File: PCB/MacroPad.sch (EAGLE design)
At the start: 42 parts, among them SW00 SWITCH-SMD-EVQP-P2602W, SW01 KEYSWITCH-PLAIN-MX-1U, SW02 KEYSWITCH-PLAIN-MX-1U, SW03 KEYSWITCH-PLAIN-MX-1U, SW04 KEYSWITCH-PLAIN-MX-1U, SW05 KEYSWITCH-PLAIN-MX-1U, SW06 KEYSWITCH-PLAIN-MX-1U, SW07 KEYSWITCH-PLAIN-MX-1U, SW08 KEYSWITCH-PLAIN-MX-1U, SW09 KEYSWITCH-PLAIN-MX-1U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

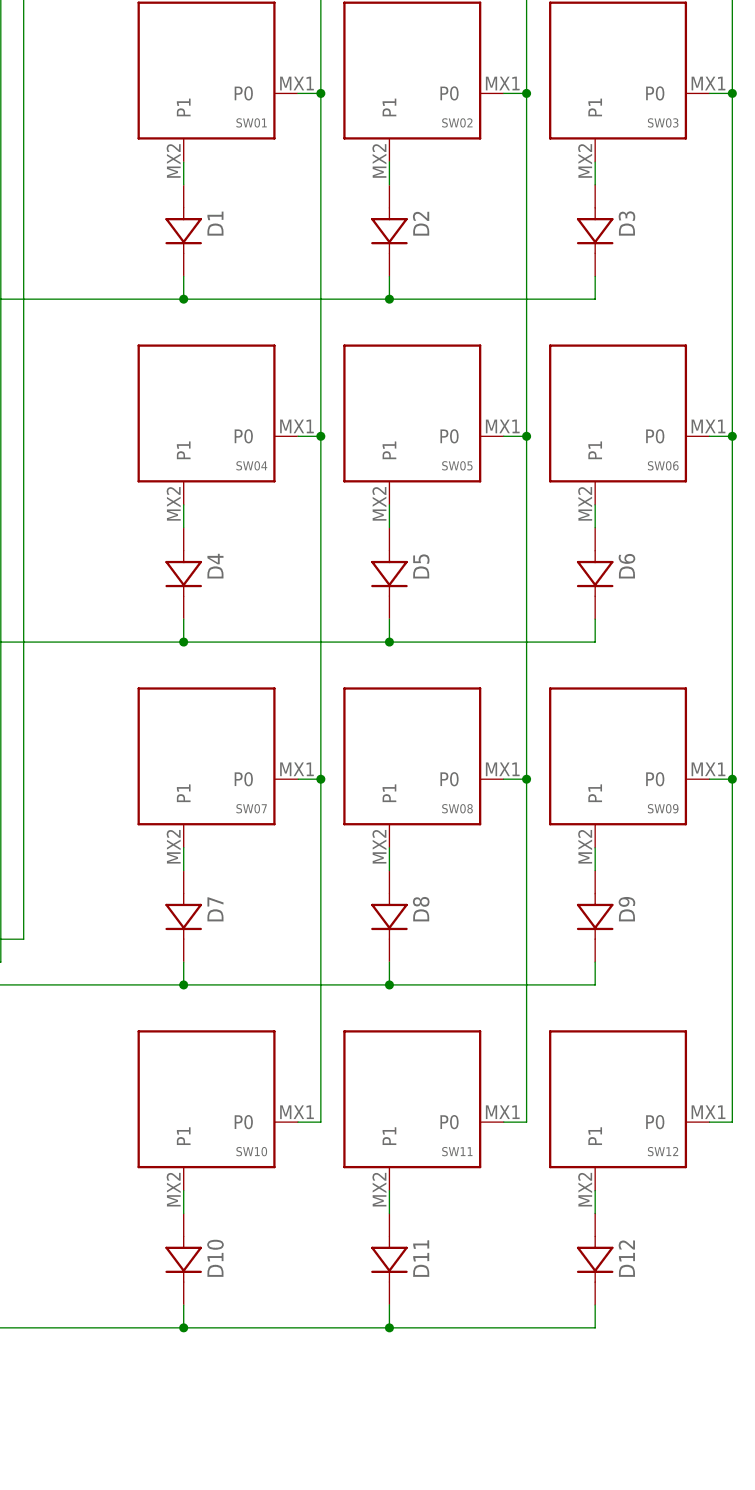
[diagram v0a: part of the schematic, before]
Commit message: Replace surface mount diodes with through hole
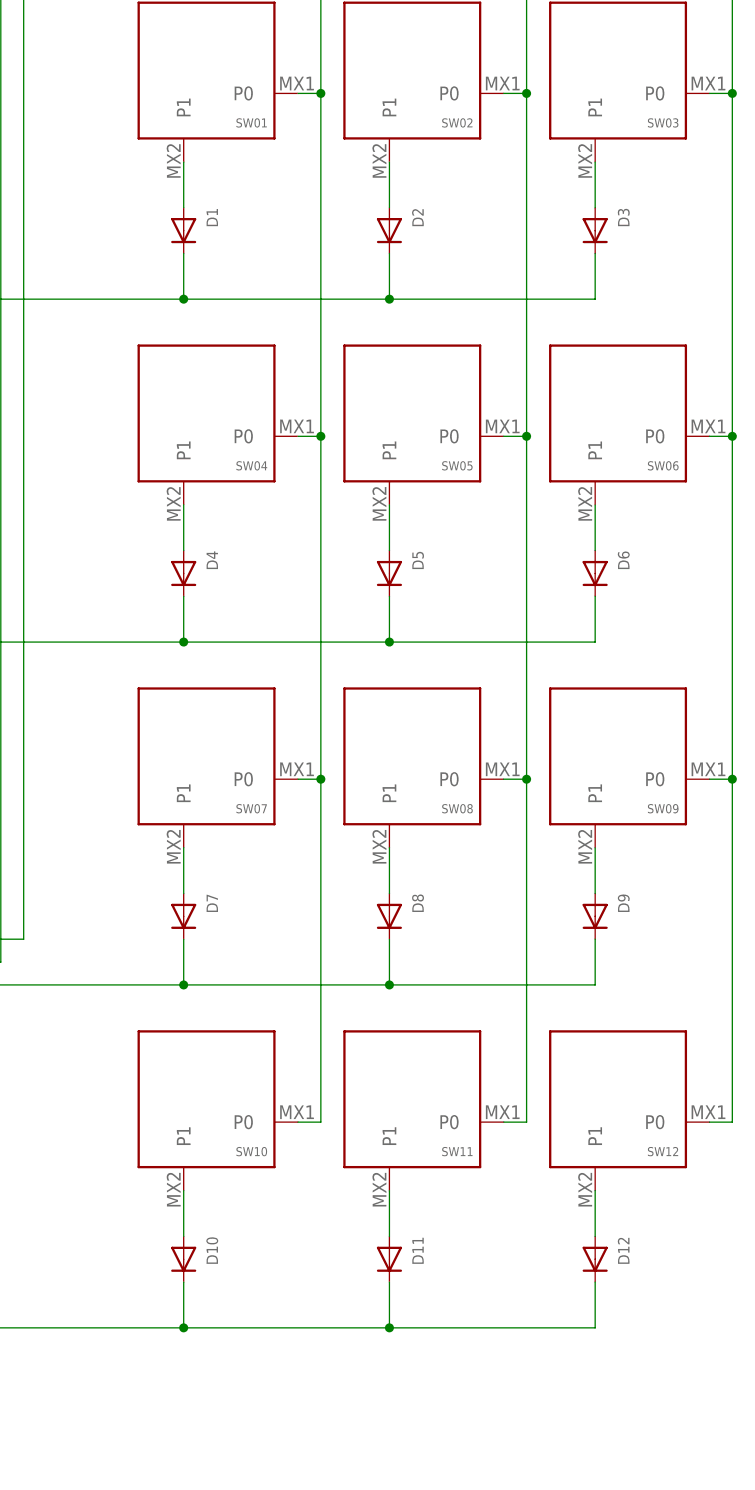
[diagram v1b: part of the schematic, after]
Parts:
- D1, D10, D11, D12, D2, D3, D4, D5, D6, D7, D8, D9: device Components:DIODE-DFN0603-2 -> adafruit:DIODEDO-1N4148; OC_NEWARK unknown -> (none)

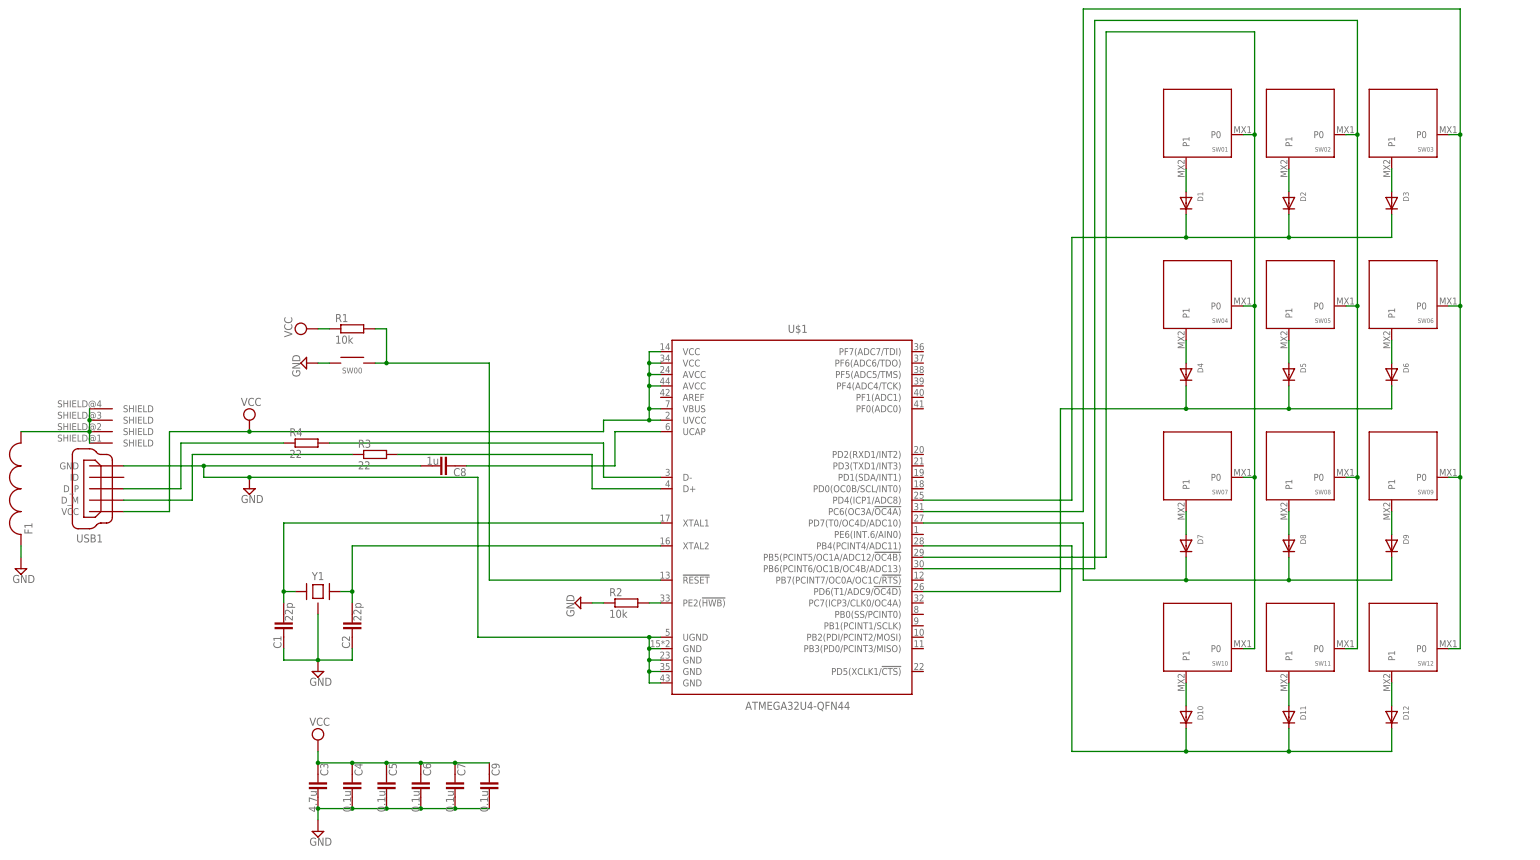
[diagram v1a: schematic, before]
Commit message: Swap GFN for TQFP Chip -- board not updated
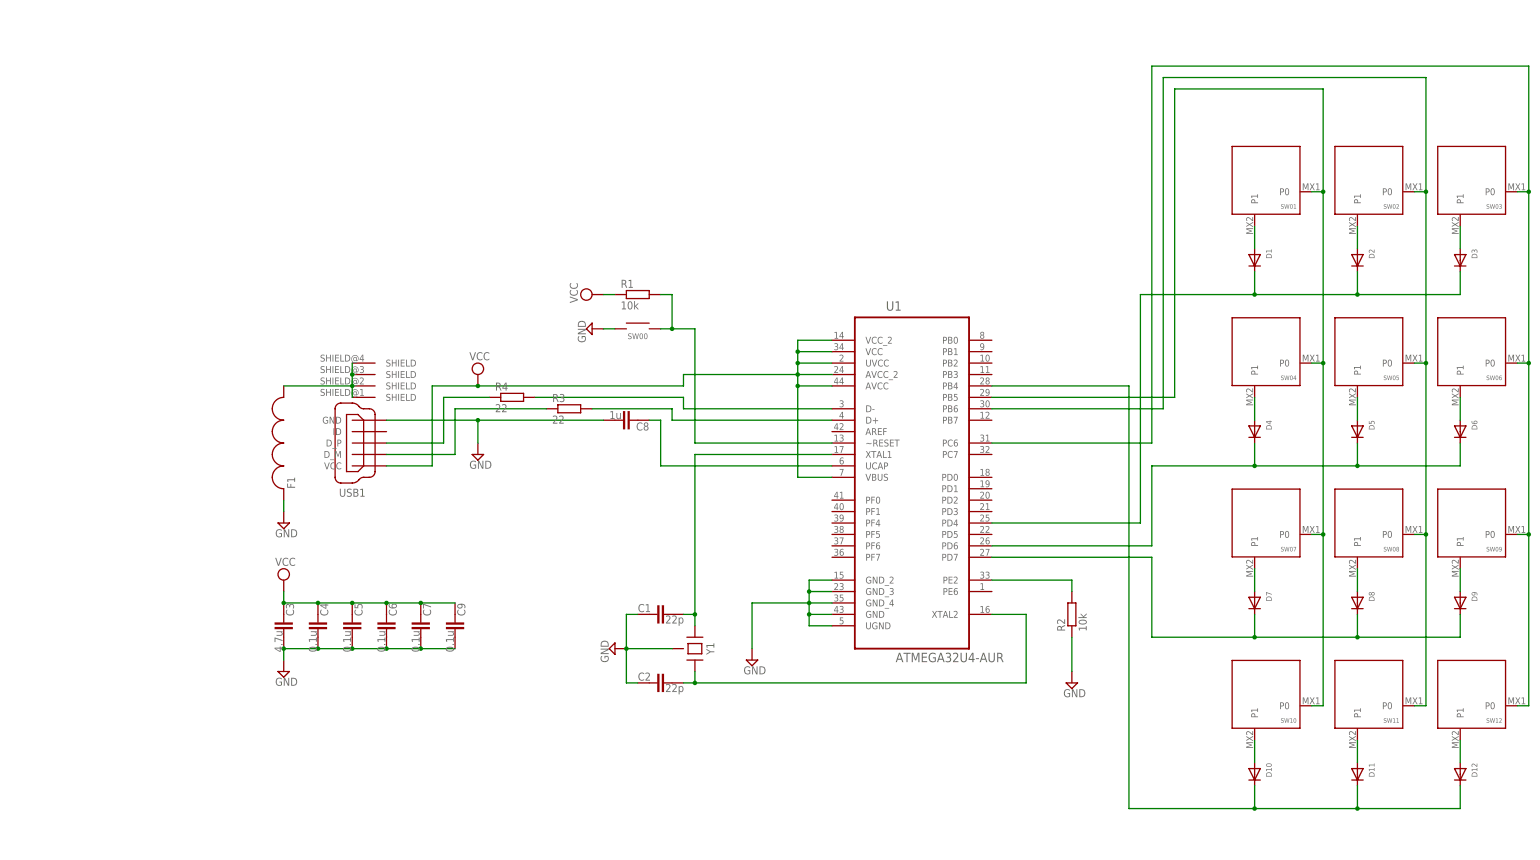
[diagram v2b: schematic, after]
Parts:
- removed U$1: ATMEGA32U4-QFN44, Controller:ATMEGA32U4-QFN44
- added U1: ATMEGA32U4-AUR, ATMEGA32U4-AUR:ATMEGA32U4-AUR
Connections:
- net GND: now also U1.GND, U1.GND_2, U1.GND_3, U1.GND_4, U1.UGND; no longer U$1.GND@15, U$1.GND@23, U$1.GND@35, U$1.GND@43, U$1.UGND
- net N$1: now also U1.XTAL2; no longer U$1.XTAL2
- net N$10: now also U1.PB5; no longer U$1.PB5(PCINT5/OC1A/ADC12/!OC4B)
- net N$14: now also U1.PD4; no longer U$1.PD4(ICP1/ADC8)
- net N$16: now also U1.PC6; no longer U$1.PC6(OC3A/!OC4A)
- net N$2: now also U1.XTAL1; no longer U$1.XTAL1
- net N$26: now also U1.PD6; no longer U$1.PD6(T1/ADC9/!OC4D)
- net N$3: now also U1.~RESET; no longer U$1.!RESET
- net N$32: now also U1.PD7; no longer U$1.PD7(T0/OC4D/ADC10)
- net N$38: now also U1.PB4; no longer U$1.PB4(PCINT4/ADC11)
- net N$4: now also U1.PE2; no longer U$1.PE2(!HWB)
- net N$40: now also U1.PB6; no longer U$1.PB6(PCINT6/OC1B/OC4B/ADC13)
- net N$6: now also U1.D-; no longer U$1.D-
- net N$8: now also U1.D+; no longer U$1.D+
- net UCAP: now also U1.UCAP; no longer U$1.UCAP
- net VCC: now also U1.AVCC, U1.AVCC_2, U1.UVCC, U1.VBUS, U1.VCC, U1.VCC_2; no longer U$1.AVCC@24, U$1.AVCC@44, U$1.UVCC, U$1.VBUS, U$1.VCC@14, U$1.VCC@34
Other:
- moved on the sheet: C1, C2, C3, C4, C5, C6, C7, C8, C9, D1, D10, D11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

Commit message: Use 5x3.2mm crystal
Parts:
- Y1: device Components:CRYSTAL-4PIN-3.2X2.5 -> Controller:CRYSTAL-4PIN-3.2X5; OC_NEWARK unknown -> (none)
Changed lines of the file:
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@@
-<attribute name="OC_NEWARK" value="unknown"/>
-</part>
-<part name="Y1" library="Components" deviceset="CRYSTAL-4PIN" device="-3.2X2.5">
-<attribute name="MF" value=""/>
-<attribute name="MPN" value=""/>
 <attribute name="OC_NEWARK" value="unknown"/>
 </part>
@@
 <part name="U1" library="ATMEGA32U4-AUR" deviceset="ATMEGA32U4-AUR" device=""/>
 <part name="SUPPLY9" library="supply2" library_urn="urn:adsk.eagle:library:372" deviceset="GND" device=""/>
+<part name="Y1" library="Controller" deviceset="CRYSTAL-4PIN" device="-3.2X5"/>
 </parts>
 <sheets>
@@
 <attribute name="MPN" x="30.48" y="81.28" size="1.778" layer="96" display="off"/>
 </instance>
-<instance part="Y1" gate="G$1" x="104.14" y="33.02" smashed="yes" rot="R270">
-<attribute name="NAME" x="106.68" y="35.56" size="1.778" layer="95" font="vector" rot="R270" align="bottom-center"/>
-<attribute name="VALUE" x="109.22" y="35.56" size="1.778" layer="96" font="vector" rot="R270" align="bottom-center"/>
-<attribute name="OC_NEWARK" x="104.14" y="33.02" size="1.778" layer="96" rot="R270" display="off"/>
-<attribute name="MF" x="104.14" y="33.02" size="1.778" layer="96" rot="R270" display="off"/>
-<attribute name="MPN" x="104.14" y="33.02" size="1.778" layer="96" rot="R270" display="off"/>
-</instance>
 <instance part="SUPPLY1" gate="GND" x="86.36" y="35.56" smashed="yes" rot="R270">
 <attribute name="VALUE" x="83.185" y="37.465" size="1.778" layer="96" rot="R270"/>
@@
 <attribute name="VALUE" x="114.935" y="29.845" size="1.778" layer="96"/>
 </instance>
+<instance part="Y1" gate="G$1" x="104.14" y="33.02" smashed="yes" rot="R270">
+<attribute name="NAME" x="106.68" y="35.56" size="1.778" layer="95" font="vector" rot="R270" align="bottom-center"/>
+<attribute name="VALUE" x="109.22" y="35.56" size="1.778" layer="96" font="vector" rot="R270" align="bottom-center"/>
+</instance>
 </instances>
 <busses>
@@
 <net name="N$1" class="0">
 <segment>
-<pinref part="Y1" gate="G$1" pin="2"/>
 <wire x1="104.14" y1="30.48" x2="104.14" y2="27.94" width="0.1524" layer="91"/>
 <junction x="104.14" y="27.94"/>
@@
 <wire x1="177.8" y1="43.18" x2="177.8" y2="27.94" width="0.1524" layer="91"/>
 <wire x1="177.8" y1="27.94" x2="104.14" y2="27.94" width="0.1524" layer="91"/>
+<pinref part="Y1" gate="G$1" pin="2"/>
 </segment>
 </net>
@@
 <segment>
 <wire x1="104.14" y1="78.74" x2="104.14" y2="43.18" width="0.1524" layer="91"/>
-<pinref part="Y1" gate="G$1" pin="1"/>
 <wire x1="104.14" y1="43.18" x2="101.6" y2="43.18" width="0.1524" layer="91"/>
 <wire x1="104.14" y1="40.64" x2="104.14" y2="43.18" width="0.1524" layer="91"/>
@@
 <pinref part="U1" gate="A" pin="XTAL1"/>
 <wire x1="104.14" y1="78.74" x2="134.62" y2="78.74" width="0.1524" layer="91"/>
+<pinref part="Y1" gate="G$1" pin="1"/>
 </segment>
 </net>
@@
 <wire x1="88.9" y1="27.94" x2="88.9" y2="35.56" width="0.1524" layer="91"/>
 <junction x="88.9" y="35.56"/>
-<pinref part="Y1" gate="G$1" pin="GND"/>
 <wire x1="99.06" y1="35.56" x2="88.9" y2="35.56" width="0.1524" layer="91"/>
 <pinref part="C1" gate="G$1" pin="1"/>
 <pinref part="C2" gate="G$1" pin="1"/>
-</segment>
-<segment>
+<pinref part="Y1" gate="G$1" pin="GND"/>
+</segment>
+<segment>

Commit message: Reroute columns to avoid vias
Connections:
- net N$10: now also U1.PC6; no longer U1.PB5
- net N$16: now also U1.PB5; no longer U1.PC6
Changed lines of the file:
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@@
 <junction x="243.84" y="60.96"/>
 <wire x1="210.82" y1="160.02" x2="243.84" y2="160.02" width="0.1524" layer="91"/>
-<pinref part="U1" gate="A" pin="PB5"/>
-<wire x1="210.82" y1="91.44" x2="210.82" y2="160.02" width="0.1524" layer="91"/>
-<wire x1="170.18" y1="91.44" x2="210.82" y2="91.44" width="0.1524" layer="91"/>
+<wire x1="210.82" y1="81.28" x2="210.82" y2="160.02" width="0.1524" layer="91"/>
+<pinref part="U1" gate="A" pin="PC6"/>
+<wire x1="170.18" y1="81.28" x2="210.82" y2="81.28" width="0.1524" layer="91"/>
 </segment>
 </net>
@@
 <junction x="289.56" y="60.96"/>
 <wire x1="205.74" y1="165.1" x2="289.56" y2="165.1" width="0.1524" layer="91"/>
-<pinref part="U1" gate="A" pin="PC6"/>
-<wire x1="170.18" y1="81.28" x2="205.74" y2="81.28" width="0.1524" layer="91"/>
-<wire x1="205.74" y1="81.28" x2="205.74" y2="165.1" width="0.1524" layer="91"/>
+<pinref part="U1" gate="A" pin="PB5"/>
+<wire x1="205.74" y1="91.44" x2="205.74" y2="165.1" width="0.1524" layer="91"/>
+<wire x1="170.18" y1="91.44" x2="205.74" y2="91.44" width="0.1524" layer="91"/>
 </segment>
 </net>

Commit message: Rename components based on board position
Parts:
- C3: value 4.7u -> 1u
- C5: value 0.1u -> 4.7u
- C8: value 1u -> 0.1u
- renumbered SW00 to RESET
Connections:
- net UCAP: now also C3.1; no longer C8.1
- net VCC: now also C8.1; no longer C3.1
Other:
- moved on the sheet: C3, C4, C5, C6, C7, C8
